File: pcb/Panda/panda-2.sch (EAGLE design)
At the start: 131 parts, among them IC1 MCP4261-103E/SL, IC2 4040D, IC3 LMC555_VSSOP, IC4 74HC00_SOIC, J1 ST-Link, J11 VIN, J12 ACC, J13 SS-52400-003, J14 Power Select, J2 SWIM, J3 ST_3.3V, J4 ST_5V, J5 USART2, J6 USB_A_SMT_FEMALE, J7 Startup Hacks, J8 Boot, K1 G6K-2P-Y, Q1 220mA/50V/3.5Ω, Q10 200mA/40V, Q11 200mA/40V, Q12 220mA/50V/3.5Ω, Q2 220mA/50V/3.5Ω, Q3 220mA/50V/3.5Ω, Q4 220mA/50V/3.5Ω, Q5 220mA/50V/3.5Ω, Q6 220mA/50V/3.5Ω, Q7 220mA/50V/3.5Ω, Q8 220mA/50V/3.5Ω, Q9 200mA/40V, SW1 Reset, SW2 Boot, U1 RASPBERRYPI4_4GB, U10 ACT1210D, U11 ACT1210D, U12 PESD2CANFD27V-T, U13 PESD2CANFD27V-T, U14 PESD2CANFD27V-T, U15 PESD2CANFD27V-T, U16 STM32H723ZGT, U17 MCP4261-103E/ML, U2 USBLC6-4SC6Y, U3 ST1L05CPU33R, U4 TLE9251VSJXUMA1, U5 TLE9251VSJXUMA1, U6 TLE9251VSJXUMA1, U7 TLE9251VSJXUMA1, U8 ACT1210D, U9 ACT1210D, X1 NX2016SA-32MHZ-EXS00A-CS06654

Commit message: Board designed with BOM, had to change 555 timer package
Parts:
- added C3: 1uF, rcl:C-EUC0402
- added D4: RST, SparkFun-LED:LED-RED0603
- added D5: BOOT, SparkFun-LED:LED-RED0603
- added JP6: VHAX, SparkFun-Jumpers:JUMPER-SMT_2_NC_PASTE_SILK
- added R35, R36: 220, rcl:R-US_R0402
- added R37: 10k, rcl:R-US_R0402
- added R38: 1k, rcl:R-US_R0402
- IC3: value LMC555_VSSOP -> LMC555_SOIC; device Tinkercad:LMC555_VSSOP -> Tinkercad:LMC555_SOIC
- R14: value 600 -> 560
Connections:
- net N$22 renamed POT_SHDN
- net N$23 renamed POT_WP
- net N$32 renamed 5VOLT_S
- removed net N$33: TP5.TP, U16.PF11
- removed net N$43: IC4.1Y, R34.2
- new net N$22: D4.A, R35.2
- new net N$23: D5.A, R36.2
- new net PI_BOOT0: J7.5, U1.GPIO27/GPIO_GEN2
- new net PI_NRST: J7.6, U1.GPIO17/GPIO_GEN0
- new net RST_DRIVE: IC4.1Y, R34.2, R35.1
- new net VHAX: IC2P.VDD, IC3.!RST, IC3.V+, IC4.VCC, JP6.2, Q11.E, R26.2, R36.1
- new net VOLT_S: C3.1, R37.1, R38.2, TP5.TP, U16.PF11
- net +3V3: now also JP6.1; no longer IC2P.VDD, IC3.!RST, IC3.V+, Q11.E, R26.2
- net BOOT_DRIVE: now also D5.C
- net GND: now also C3.2, D4.C, R38.1
- net VIN: now also R37.2
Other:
- moved on the sheet: TP4, TP5

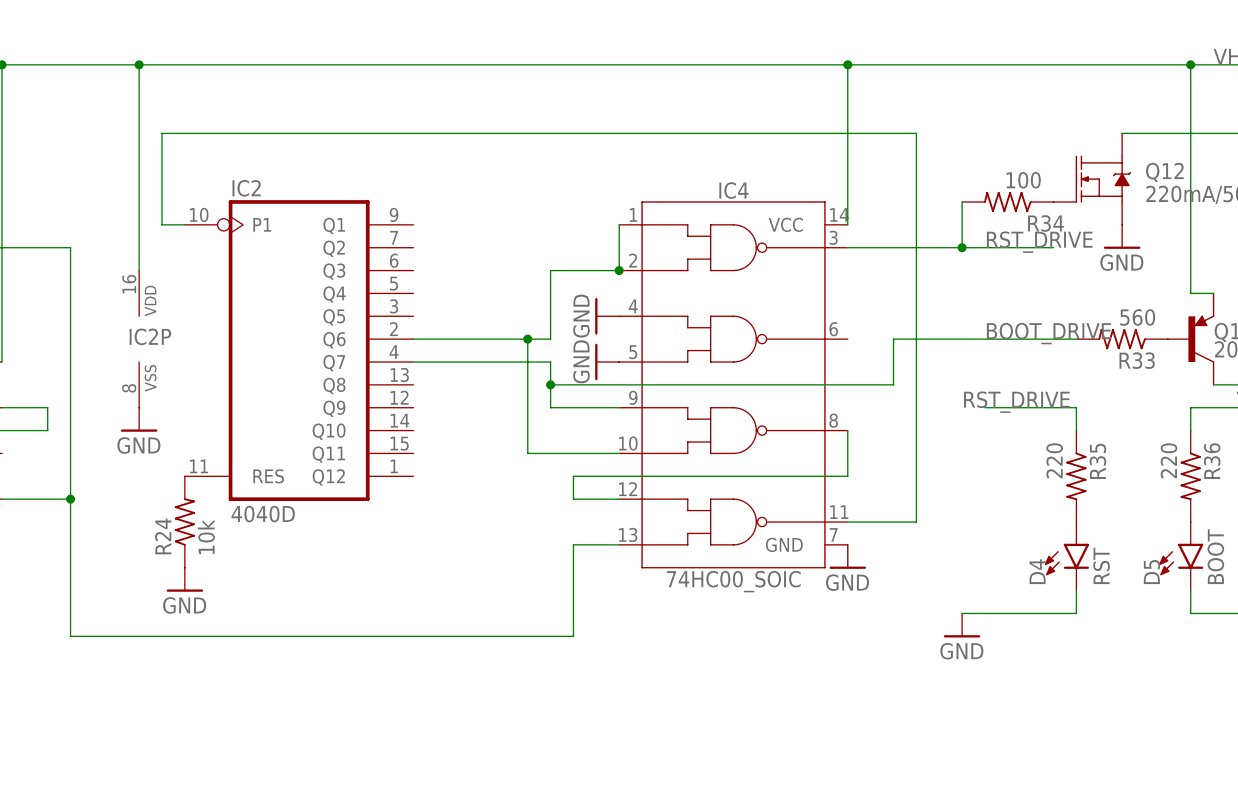
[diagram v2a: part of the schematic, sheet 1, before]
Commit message: PCB nearing completion, added links and changed some of the 555 timer logic
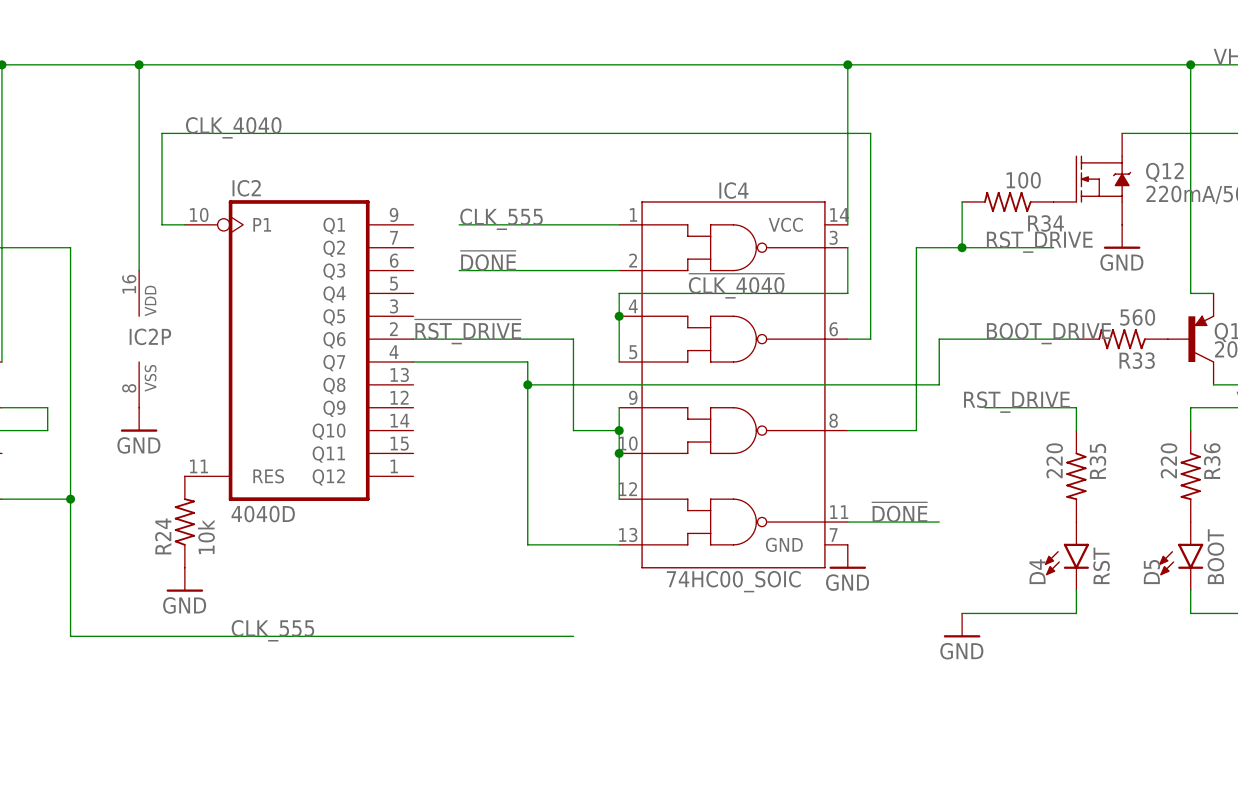
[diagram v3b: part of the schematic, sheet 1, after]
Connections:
- removed net N$36: IC3.OUT, IC4.4B, R32.1
- removed net N$39: IC2A.P1, IC4.4Y
- removed net N$41: IC2A.Q6, IC4.1A, IC4.1B, IC4.3B
- removed net N$42: IC4.3Y, IC4.4A
- new net !CLK_4040: IC4.1Y, IC4.2A, IC4.2B
- new net !DONE: IC4.1B, IC4.4Y
- new net !RST_DRIVE: IC2A.Q6, IC4.3A, IC4.3B, IC4.4A
- new net CLK_4040: IC2A.P1, IC4.2Y
- new net CLK_555: IC3.OUT, IC4.1A, R32.1
- net BOOT_DRIVE: now also IC4.4B; no longer IC4.3A
- net GND: no longer IC4.2A, IC4.2B
- net RST_DRIVE: now also IC4.3Y; no longer IC4.1Y
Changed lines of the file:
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@@
 <part name="SW2" library="SparkFun-Switches" library_urn="urn:adsk.eagle:library:535" deviceset="MOMENTARY-SWITCH-SPST" device="-PTH-6.0MM" package3d_urn="urn:adsk.eagle:package:40163/1" value="Boot"/>
 <part name="GND71" library="supply1" library_urn="urn:adsk.eagle:library:371" deviceset="GND" device=""/>
-<part name="GND72" library="supply1" library_urn="urn:adsk.eagle:library:371" deviceset="GND" device=""/>
-<part name="GND73" library="supply1" library_urn="urn:adsk.eagle:library:371" deviceset="GND" device=""/>
 <part name="GND74" library="supply1" library_urn="urn:adsk.eagle:library:371" deviceset="GND" device=""/>
 <part name="J7" library="SparkFun-Connectors" library_urn="urn:adsk.eagle:library:513" deviceset="CONN_03X2" device="FEMALE" package3d_urn="urn:adsk.eagle:package:38016/1" value="Startup Hacks"/>
@@
 <instance part="GND71" gate="1" x="205.74" y="180.34" smashed="yes">
 <attribute name="VALUE" x="203.2" y="177.8" size="1.778" layer="96"/>
-</instance>
-<instance part="GND72" gate="1" x="177.8" y="203.2" smashed="yes" rot="R270">
-<attribute name="VALUE" x="175.26" y="205.74" size="1.778" layer="96" rot="R270"/>
-</instance>
-<instance part="GND73" gate="1" x="177.8" y="208.28" smashed="yes" rot="R270">
-<attribute name="VALUE" x="175.26" y="210.82" size="1.778" layer="96" rot="R270"/>
 </instance>
 <instance part="IC2" gate="P" x="127" y="205.74" smashed="yes">
@@
 </segment>
 <segment>
-<pinref part="IC4" gate="G$1" pin="2B"/>
-<pinref part="GND72" gate="1" pin="GND"/>
-</segment>
-<segment>
-<pinref part="IC4" gate="G$1" pin="2A"/>
-<pinref part="GND73" gate="1" pin="GND"/>
-</segment>
-<segment>
 <pinref part="IC2" gate="P" pin="VSS"/>
 <pinref part="GND74" gate="1" pin="GND"/>
@@
 </segment>
 </net>
-<net name="N$36" class="0">
+<net name="CLK_555" class="0">
 <segment>
 <wire x1="111.76" y1="187.96" x2="119.38" y2="187.96" width="0.1524" layer="91"/>
@@
 <wire x1="119.38" y1="172.72" x2="175.26" y2="172.72" width="0.1524" layer="91"/>
 <junction x="119.38" y="187.96"/>
-<pinref part="IC4" gate="G$1" pin="4B"/>
-<wire x1="175.26" y1="172.72" x2="175.26" y2="182.88" width="0.1524" layer="91"/>
-<wire x1="175.26" y1="182.88" x2="180.34" y2="182.88" width="0.1524" layer="91"/>
 <pinref part="IC3" gate="G$1" pin="OUT"/>
+<label x="137.16" y="172.72" size="1.778" layer="95"/>
+</segment>
+<segment>
+<pinref part="IC4" gate="G$1" pin="1A"/>
+<wire x1="180.34" y1="218.44" x2="162.56" y2="218.44" width="0.1524" layer="91"/>
+<label x="162.56" y="218.44" size="1.778" layer="95"/>
 </segment>
 </net>
@@
 </segment>
 </net>
-<net name="N$39" class="0">
-<segment>
-<wire x1="213.36" y1="185.42" x2="213.36" y2="228.6" width="0.1524" layer="91"/>
-<wire x1="213.36" y1="228.6" x2="129.54" y2="228.6" width="0.1524" layer="91"/>
+<net name="CLK_4040" class="0">
+<segment>
 <pinref part="IC2" gate="A" pin="P1"/>
+<wire x1="208.28" y1="228.6" x2="129.54" y2="228.6" width="0.1524" layer="91"/>
 <wire x1="129.54" y1="228.6" x2="129.54" y2="218.44" width="0.1524" layer="91"/>
 <wire x1="129.54" y1="218.44" x2="132.08" y2="218.44" width="0.1524" layer="91"/>
-<pinref part="IC4" gate="G$1" pin="4Y"/>
-<wire x1="205.74" y1="185.42" x2="213.36" y2="185.42" width="0.1524" layer="91"/>
-</segment>
-</net>
-<net name="N$41" class="0">
+<label x="132.08" y="228.6" size="1.778" layer="95"/>
+<pinref part="IC4" gate="G$1" pin="2Y"/>
+<wire x1="205.74" y1="205.74" x2="208.28" y2="205.74" width="0.1524" layer="91"/>
+<wire x1="208.28" y1="205.74" x2="208.28" y2="228.6" width="0.1524" layer="91"/>
+</segment>
+</net>
+<net name="!RST_DRIVE" class="0">
 <segment>
 <pinref part="IC2" gate="A" pin="Q6"/>
-<wire x1="157.48" y1="205.74" x2="170.18" y2="205.74" width="0.1524" layer="91"/>
-<pinref part="IC4" gate="G$1" pin="1B"/>
-<wire x1="170.18" y1="205.74" x2="172.72" y2="205.74" width="0.1524" layer="91"/>
-<wire x1="172.72" y1="205.74" x2="172.72" y2="213.36" width="0.1524" layer="91"/>
-<wire x1="172.72" y1="213.36" x2="180.34" y2="213.36" width="0.1524" layer="91"/>
-<pinref part="IC4" gate="G$1" pin="1A"/>
-<wire x1="180.34" y1="218.44" x2="180.34" y2="213.36" width="0.1524" layer="91"/>
-<junction x="180.34" y="213.36"/>
-<wire x1="170.18" y1="205.74" x2="170.18" y2="193.04" width="0.1524" layer="91"/>
-<junction x="170.18" y="205.74"/>
+<wire x1="157.48" y1="205.74" x2="175.26" y2="205.74" width="0.1524" layer="91"/>
+<wire x1="175.26" y1="205.74" x2="175.26" y2="195.58" width="0.1524" layer="91"/>
+<label x="157.48" y="205.74" size="1.778" layer="95"/>
+<pinref part="IC4" gate="G$1" pin="3A"/>
 <pinref part="IC4" gate="G$1" pin="3B"/>
-<wire x1="170.18" y1="193.04" x2="180.34" y2="193.04" width="0.1524" layer="91"/>
-</segment>
-</net>
-<net name="N$42" class="0">
-<segment>
-<pinref part="IC4" gate="G$1" pin="3Y"/>
-<wire x1="205.74" y1="195.58" x2="205.74" y2="190.5" width="0.1524" layer="91"/>
-<wire x1="205.74" y1="190.5" x2="175.26" y2="190.5" width="0.1524" layer="91"/>
-<wire x1="175.26" y1="190.5" x2="175.26" y2="187.96" width="0.1524" layer="91"/>
+<wire x1="180.34" y1="198.12" x2="180.34" y2="195.58" width="0.1524" layer="91"/>
+<wire x1="180.34" y1="195.58" x2="180.34" y2="193.04" width="0.1524" layer="91"/>
+<wire x1="175.26" y1="195.58" x2="180.34" y2="195.58" width="0.1524" layer="91"/>
+<junction x="180.34" y="195.58"/>
 <pinref part="IC4" gate="G$1" pin="4A"/>
-<wire x1="175.26" y1="187.96" x2="180.34" y2="187.96" width="0.1524" layer="91"/>
+<wire x1="180.34" y1="193.04" x2="180.34" y2="187.96" width="0.1524" layer="91"/>
+<junction x="180.34" y="193.04"/>
 </segment>
 </net>
@@
 <pinref part="R33" gate="G$1" pin="2"/>
 <pinref part="IC2" gate="A" pin="Q7"/>
-<wire x1="210.82" y1="205.74" x2="231.14" y2="205.74" width="0.1524" layer="91"/>
-<wire x1="157.48" y1="203.2" x2="172.72" y2="203.2" width="0.1524" layer="91"/>
-<pinref part="IC4" gate="G$1" pin="3A"/>
-<wire x1="180.34" y1="198.12" x2="172.72" y2="198.12" width="0.1524" layer="91"/>
-<wire x1="172.72" y1="198.12" x2="172.72" y2="200.66" width="0.1524" layer="91"/>
-<wire x1="172.72" y1="200.66" x2="172.72" y2="203.2" width="0.1524" layer="91"/>
-<wire x1="172.72" y1="200.66" x2="210.82" y2="200.66" width="0.1524" layer="91"/>
-<wire x1="210.82" y1="200.66" x2="210.82" y2="205.74" width="0.1524" layer="91"/>
-<junction x="172.72" y="200.66"/>
+<wire x1="215.9" y1="205.74" x2="231.14" y2="205.74" width="0.1524" layer="91"/>
+<wire x1="157.48" y1="203.2" x2="170.18" y2="203.2" width="0.1524" layer="91"/>
+<wire x1="170.18" y1="200.66" x2="170.18" y2="203.2" width="0.1524" layer="91"/>
+<wire x1="170.18" y1="200.66" x2="215.9" y2="200.66" width="0.1524" layer="91"/>
+<wire x1="215.9" y1="200.66" x2="215.9" y2="205.74" width="0.1524" layer="91"/>
+<wire x1="170.18" y1="200.66" x2="170.18" y2="182.88" width="0.1524" layer="91"/>
+<junction x="170.18" y="200.66"/>
+<pinref part="IC4" gate="G$1" pin="4B"/>
+<wire x1="170.18" y1="182.88" x2="180.34" y2="182.88" width="0.1524" layer="91"/>
 </segment>
 <segment>
@@
 <net name="RST_DRIVE" class="0">
 <segment>
-<pinref part="IC4" gate="G$1" pin="1Y"/>
 <pinref part="R34" gate="G$1" pin="2"/>
-<wire x1="205.74" y1="215.9" x2="218.44" y2="215.9" width="0.1524" layer="91"/>
 <wire x1="218.44" y1="215.9" x2="218.44" y2="220.98" width="0.1524" layer="91"/>
 <wire x1="218.44" y1="215.9" x2="228.6" y2="215.9" width="0.1524" layer="91"/>
+<label x="220.98" y="215.9" size="1.778" layer="95"/>
+<wire x1="213.36" y1="195.58" x2="213.36" y2="215.9" width="0.1524" layer="91"/>
+<wire x1="218.44" y1="215.9" x2="213.36" y2="215.9" width="0.1524" layer="91"/>
 <junction x="218.44" y="215.9"/>
-<label x="220.98" y="215.9" size="1.778" layer="95"/>
+<pinref part="IC4" gate="G$1" pin="3Y"/>
+<wire x1="213.36" y1="195.58" x2="205.74" y2="195.58" width="0.1524" layer="91"/>
 </segment>
 <segment>
@@
 </segment>
 </net>
+<net name="!CLK_4040" class="0">
+<segment>
+<pinref part="IC4" gate="G$1" pin="2B"/>
+<pinref part="IC4" gate="G$1" pin="2A"/>
+<wire x1="180.34" y1="203.2" x2="180.34" y2="208.28" width="0.1524" layer="91"/>
+<wire x1="180.34" y1="208.28" x2="180.34" y2="210.82" width="0.1524" layer="91"/>
+<junction x="180.34" y="208.28"/>
+<wire x1="180.34" y1="210.82" x2="205.74" y2="210.82" width="0.1524" layer="91"/>
+<pinref part="IC4" gate="G$1" pin="1Y"/>
+<wire x1="205.74" y1="210.82" x2="205.74" y2="215.9" width="0.1524" layer="91"/>
+<label x="187.96" y="210.82" size="1.778" layer="95"/>
+</segment>
+</net>
+<net name="!DONE" class="0">
+<segment>
+<pinref part="IC4" gate="G$1" pin="1B"/>
+<wire x1="180.34" y1="213.36" x2="162.56" y2="213.36" width="0.1524" layer="91"/>
+<label x="162.56" y="213.36" size="1.778" layer="95"/>
+</segment>
+<segment>
+<pinref part="IC4" gate="G$1" pin="4Y"/>
+<wire x1="205.74" y1="185.42" x2="215.9" y2="185.42" width="0.1524" layer="91"/>
+<label x="208.28" y="185.42" size="1.778" layer="95"/>
+</segment>
+</net>

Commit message: the mattHat v1.0 as submitted for 110 pcbs to be built by Surface Art
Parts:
- R26: value 220k -> DNP
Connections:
- net N$46 renamed BOARD_BOOT0
- net N$47 renamed BOARD_NRST
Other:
- moved on the sheet: R34
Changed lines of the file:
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@@
 <part name="C2" library="rcl" library_urn="urn:adsk.eagle:library:334" deviceset="C-EU" device="C0402" package3d_urn="urn:adsk.eagle:package:23626/2" value="100nF"/>
 <part name="GND67" library="supply1" library_urn="urn:adsk.eagle:library:371" deviceset="GND" device=""/>
-<part name="R26" library="rcl" library_urn="urn:adsk.eagle:library:334" deviceset="R-US_" device="R0402" package3d_urn="urn:adsk.eagle:package:23547/3" value="220k"/>
+<part name="R26" library="rcl" library_urn="urn:adsk.eagle:library:334" deviceset="R-US_" device="R0402" package3d_urn="urn:adsk.eagle:package:23547/3" value="DNP"/>
 <part name="R32" library="rcl" library_urn="urn:adsk.eagle:library:334" deviceset="R-US_" device="R0402" package3d_urn="urn:adsk.eagle:package:23547/3" value="2.4k"/>
 <part name="GND68" library="supply1" library_urn="urn:adsk.eagle:library:371" deviceset="GND" device=""/>
@@
 <attribute name="VALUE" x="238.76" y="220.98" size="1.778" layer="96" font="vector"/>
 </instance>
-<instance part="R34" gate="G$1" x="223.52" y="220.98" smashed="yes" rot="R180">
-<attribute name="NAME" x="229.87" y="219.4814" size="1.778" layer="95" rot="R180"/>
+<instance part="R34" gate="G$1" x="220.98" y="220.98" smashed="yes" rot="R180">
+<attribute name="NAME" x="219.71" y="224.5614" size="1.778" layer="95" rot="R180"/>
 <attribute name="VALUE" x="227.33" y="224.282" size="1.778" layer="96" rot="R180"/>
 </instance>
@@
 <net name="BOOT_DRIVE" class="0">
 <segment>
-<label x="220.98" y="205.74" size="1.778" layer="95"/>
+<label x="215.9" y="205.74" size="1.778" layer="95"/>
 <pinref part="R33" gate="G$1" pin="2"/>
 <pinref part="IC2" gate="A" pin="Q7"/>
@@
 <pinref part="Q12" gate="NMOS" pin="G"/>
 <pinref part="R34" gate="G$1" pin="1"/>
+<wire x1="226.06" y1="220.98" x2="228.6" y2="220.98" width="0.1524" layer="91"/>
 </segment>
 </net>
@@
 <segment>
 <pinref part="R34" gate="G$1" pin="2"/>
-<wire x1="218.44" y1="215.9" x2="218.44" y2="220.98" width="0.1524" layer="91"/>
-<wire x1="218.44" y1="215.9" x2="228.6" y2="215.9" width="0.1524" layer="91"/>
-<label x="220.98" y="215.9" size="1.778" layer="95"/>
+<wire x1="215.9" y1="215.9" x2="215.9" y2="220.98" width="0.1524" layer="91"/>
+<wire x1="215.9" y1="215.9" x2="226.06" y2="215.9" width="0.1524" layer="91"/>
+<label x="218.44" y="215.9" size="1.778" layer="95"/>
 <wire x1="213.36" y1="195.58" x2="213.36" y2="215.9" width="0.1524" layer="91"/>
-<wire x1="218.44" y1="215.9" x2="213.36" y2="215.9" width="0.1524" layer="91"/>
-<junction x="218.44" y="215.9"/>
+<wire x1="215.9" y1="215.9" x2="213.36" y2="215.9" width="0.1524" layer="91"/>
+<junction x="215.9" y="215.9"/>
 <pinref part="IC4" gate="G$1" pin="3Y"/>
 <wire x1="213.36" y1="195.58" x2="205.74" y2="195.58" width="0.1524" layer="91"/>
@@
 </segment>
 </net>
-<net name="N$46" class="0">
+<net name="BOARD_BOOT0" class="0">
 <segment>
 <pinref part="Q11" gate="G$1" pin="C"/>
@@
 <wire x1="246.38" y1="200.66" x2="281.94" y2="200.66" width="0.1524" layer="91"/>
 <wire x1="281.94" y1="200.66" x2="281.94" y2="203.2" width="0.1524" layer="91"/>
-</segment>
-</net>
-<net name="N$47" class="0">
+<label x="259.08" y="200.66" size="1.778" layer="95"/>
+</segment>
+</net>
+<net name="BOARD_NRST" class="0">
 <segment>
 <pinref part="Q12" gate="NMOS" pin="D"/>
@@
 <wire x1="236.22" y1="228.6" x2="281.94" y2="228.6" width="0.1524" layer="91"/>
 <wire x1="281.94" y1="228.6" x2="281.94" y2="218.44" width="0.1524" layer="91"/>
-</segment>
-</net>
+<label x="259.08" y="228.6" size="1.778" layer="95"/>
+</segment>
+</net>
